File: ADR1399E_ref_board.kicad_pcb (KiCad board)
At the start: 4 copper layers, 119 x 60 mm, 103 parts, among them IC1 ADP7142ARDZ-R7, J1 Conn_01x02_Pin, J2 USB_C_Receptacle_PowerOnly_6P, J3 Conn_Coaxial, J4 S4B-XH-A, P1 JST_B2P_VH, Q1 MMBT3906, Q2 2N7002, U2 TPS61085DGK, U3 OPA182IDR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

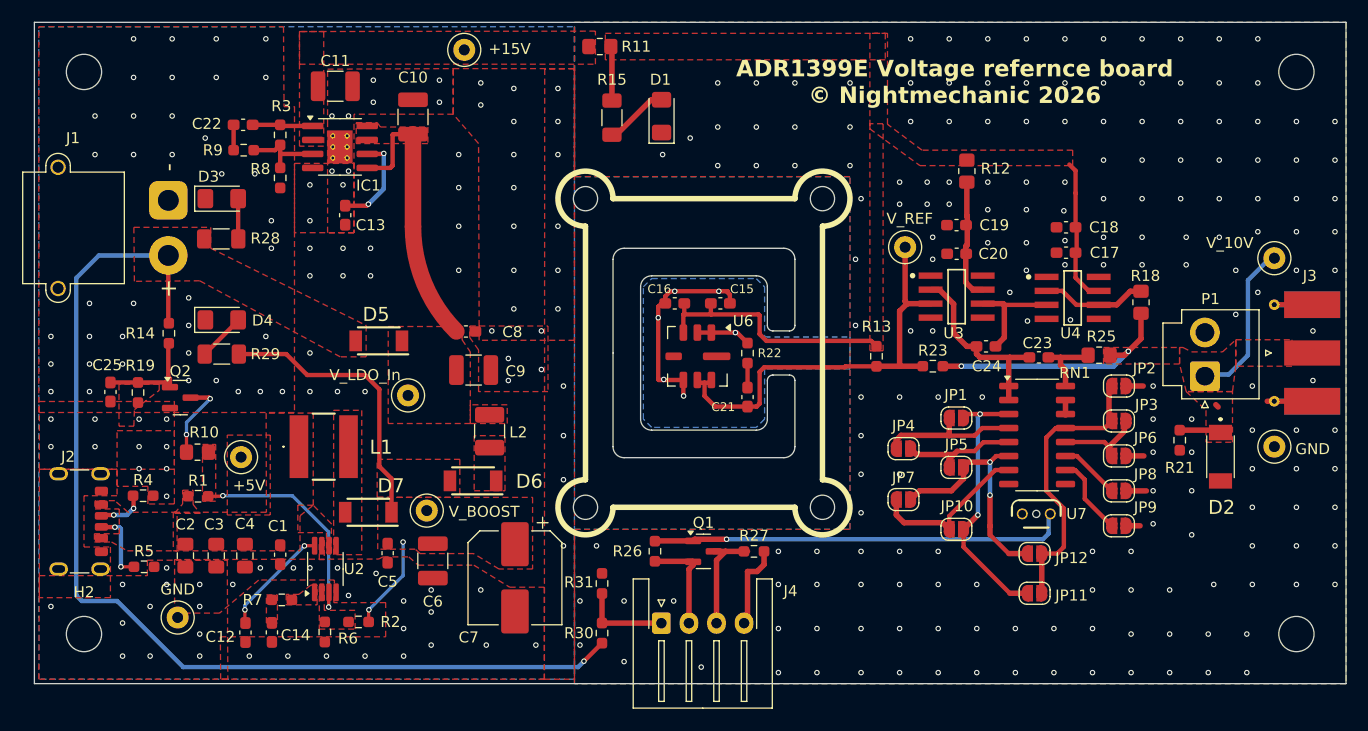
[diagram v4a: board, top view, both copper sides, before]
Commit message: Updated sllkscreen (logo etc.)
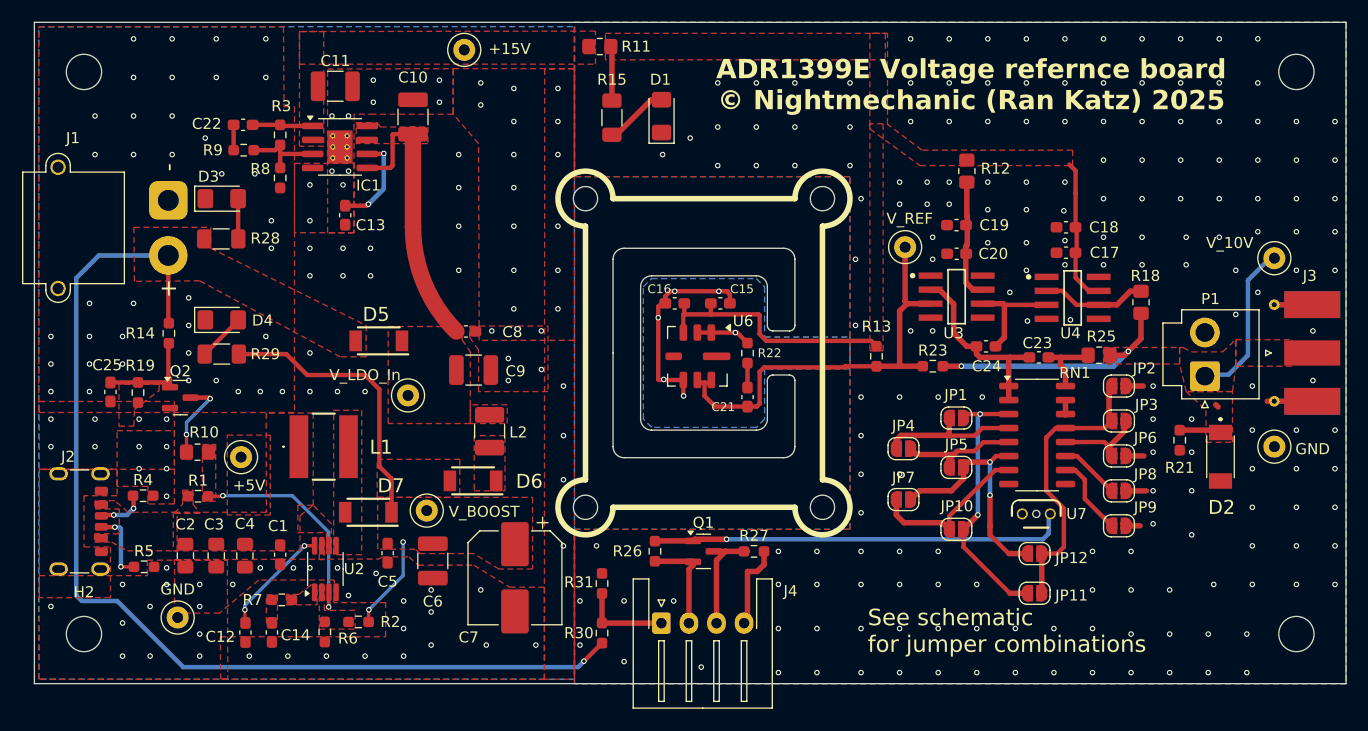
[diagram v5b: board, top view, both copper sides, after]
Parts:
- added G***: LOGO, nightmechanic_pcb:nightmechanic_logo, B.Cu at (59.5, 91.0)
- added REF**: OSHW-Logo2_24.3x20mm_SilkScreen, Symbol:OSHW-Logo2_24.3x20mm_SilkScreen, B.Cu at (124.5, 92.1)
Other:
- board text added: "ADR1399E Voltage refernce board © Nightmechanic (Ran Katz) 2025"
- board text added: "See schematic for jumper combinations"
- board text added: "© Nightmechanic 2025"
- board text removed: "ADR1399E Voltage refernce board © Nightmechanic 2026"
